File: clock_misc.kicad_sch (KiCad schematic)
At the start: 18 parts, among them J11 SPRING_CONTACT, J12 SPRING_CONTACT, J13 SPRING_CONTACT, J14 SPRING_CONTACT, J15 SPRING_CONTACT, J16 SPRING_CONTACT, Y1 Osc60MHz

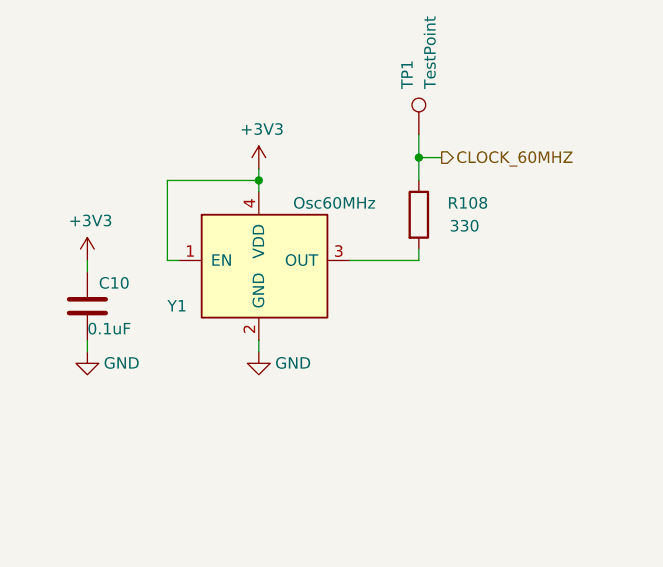
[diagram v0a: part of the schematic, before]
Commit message: Clean up schematic
- Renumber Pmod signal names to match silkscreen labels
- Clean up FPGA symbol
- Clean up PHY symbol
- Add title block to newer sheets
- Fix horizontal line in LED sheet
- Improve various label positions
- Update data sheet fields
- Renumber pages
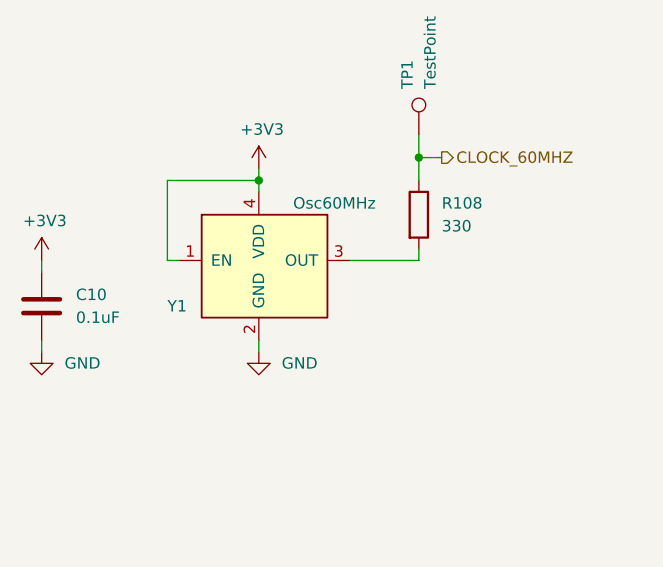
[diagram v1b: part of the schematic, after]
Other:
- company: (none) -> Copyright 2019-2023 Great Scott Gadgets
- title: (none) -> Cynthion
- moved on the sheet: C10
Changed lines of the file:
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@@
 (kicad_sch (version 20230121) (generator eeschema)
   (paper "A4")
+  (title_block
+    (title "Cynthion")
+    (date "${DATE}")
+    (rev "${VERSION}")
+    (company "Copyright 2019-2023 Great Scott Gadgets")
+    (comment 1 "Licensed under the CERN-OHL-P v2")
+  )
   (junction (at 73.66 67.31) (diameter 0) (color 0 0 0 0)
   )
@@
     (stroke (width 0) (type default))
   )
-  (wire (pts (xy 54.61 85.09) (xy 54.61 86.36))
+  (wire (pts (xy 49.53 85.09) (xy 49.53 86.36))
     (stroke (width 0) (type default))
   )
@@
     (stroke (width 0) (type default))
   )
-  (wire (pts (xy 54.61 76.2) (xy 54.61 77.47))
+  (wire (pts (xy 49.53 76.2) (xy 49.53 77.47))
     (stroke (width 0) (type default))
   )
@@
     (effects (font (size 1.27 1.27)) (justify left))
   )
-  (symbol (lib_id "Device:C") (at 54.61 81.28 0) (unit 1)
-    (in_bom yes) (on_board yes) (dnp no)
-    (property "Reference" "C10" (at 55.88 78.74 0)
-      (effects (font (size 1.27 1.27)) (justify left))
-    )
-    (property "Value" "0.1uF" (at 54.61 83.82 0)
-      (effects (font (size 1.27 1.27)) (justify left))
-    )
-    (property "Footprint" "Capacitor_SMD:C_0402_1005Metric" (at 55.5752 85.09 0)
-      (effects (font (size 1.27 1.27)) hide)
-    )
-    (property "Datasheet" "~" (at 54.61 81.28 0)
-      (effects (font (size 1.27 1.27)) hide)
-    )
-    (property "Part Number" "CL05A104KA5NNNC" (at 54.61 81.28 0)
-      (effects (font (size 1.27 1.27)) hide)
-    )
-    (property "Substitution" "any equivalent" (at 54.61 81.28 0)
-      (effects (font (size 1.27 1.27)) hide)
-    )
-    (property "Description" "CAP CER 0.1UF 25V X5R 0402" (at 54.61 81.28 0)
-      (effects (font (size 1.27 1.27)) hide)
-    )
-    (property "Manufacturer" "Samsung" (at 54.61 81.28 0)
+  (symbol (lib_id "Device:C") (at 49.53 81.28 0) (unit 1)
+    (in_bom yes) (on_board yes) (dnp no) (fields_autoplaced)
+    (property "Reference" "C10" (at 53.34 80.01 0)
+      (effects (font (size 1.27 1.27)) (justify left))
+    )
+    (property "Value" "0.1uF" (at 53.34 82.55 0)
+      (effects (font (size 1.27 1.27)) (justify left))
+    )
+    (property "Footprint" "Capacitor_SMD:C_0402_1005Metric" (at 50.4952 85.09 0)
+      (effects (font (size 1.27 1.27)) hide)
+    )
+    (property "Datasheet" "~" (at 49.53 81.28 0)
+      (effects (font (size 1.27 1.27)) hide)
+    )
+    (property "Part Number" "CL05A104KA5NNNC" (at 49.53 81.28 0)
+      (effects (font (size 1.27 1.27)) hide)
+    )
+    (property "Substitution" "any equivalent" (at 49.53 81.28 0)
+      (effects (font (size 1.27 1.27)) hide)
+    )
+    (property "Description" "CAP CER 0.1UF 25V X5R 0402" (at 49.53 81.28 0)
+      (effects (font (size 1.27 1.27)) hide)
+    )
+    (property "Manufacturer" "Samsung" (at 49.53 81.28 0)
       (effects (font (size 1.27 1.27)) hide)
     )
@@
       (effects (font (size 1.27 1.27)) hide)
     )
-    (property "Datasheet" "" (at 67.31 71.12 0)
+    (property "Datasheet" "https://www.sitime.com/datasheet/SiT1602" (at 67.31 71.12 0)
       (effects (font (size 1.27 1.27)) hide)
     )
@@
   )
   (symbol (lib_id "Device:R") (at 91.44 71.12 0) (unit 1)
-    (in_bom yes) (on_board yes) (dnp no)
-    (property "Reference" "R108" (at 94.615 69.85 0)
-      (effects (font (size 1.27 1.27)) (justify left))
-    )
-    (property "Value" "330" (at 96.52 72.39 0)
-      (effects (font (size 1.27 1.27)))
+    (in_bom yes) (on_board yes) (dnp no) (fields_autoplaced)
+    (property "Reference" "R108" (at 93.98 69.85 0)
+      (effects (font (size 1.27 1.27)) (justify left))
+    )
+    (property "Value" "330" (at 93.98 72.39 0)
+      (effects (font (size 1.27 1.27)) (justify left))
     )
     (property "Footprint" "Resistor_SMD:R_0402_1005Metric" (at 89.662 71.12 90)
@@
   )
   (symbol (lib_id "power:GND") (at 73.66 86.36 0) (unit 1)
-    (in_bom yes) (on_board yes) (dnp no)
+    (in_bom yes) (on_board yes) (dnp no) (fields_autoplaced)
     (property "Reference" "#PWR086" (at 73.66 92.71 0)
       (effects (font (size 1.27 1.27)) hide)
     )
-    (property "Value" "GND" (at 77.47 87.63 0)
-      (effects (font (size 1.27 1.27)))
+    (property "Value" "GND" (at 76.2 87.63 0)
+      (effects (font (size 1.27 1.27)) (justify left))
     )
     (property "Footprint" "" (at 73.66 86.36 0)
@@
     )
   )
-  (symbol (lib_id "power:GND") (at 54.61 86.36 0) (unit 1)
-    (in_bom yes) (on_board yes) (dnp no)
-    (property "Reference" "#PWR0174" (at 54.61 92.71 0)
-      (effects (font (size 1.27 1.27)) hide)
-    )
-    (property "Value" "GND" (at 58.42 87.63 0)
-      (effects (font (size 1.27 1.27)))
-    )
-    (property "Footprint" "" (at 54.61 86.36 0)
-      (effects (font (size 1.27 1.27)) hide)
-    )
-    (property "Datasheet" "" (at 54.61 86.36 0)
+  (symbol (lib_id "power:GND") (at 49.53 86.36 0) (unit 1)
+    (in_bom yes) (on_board yes) (dnp no) (fields_autoplaced)
+    (property "Reference" "#PWR0174" (at 49.53 92.71 0)
+      (effects (font (size 1.27 1.27)) hide)
+    )
+    (property "Value" "GND" (at 52.07 87.63 0)
+      (effects (font (size 1.27 1.27)) (justify left))
+    )
+    (property "Footprint" "" (at 49.53 86.36 0)
+      (effects (font (size 1.27 1.27)) hide)
+    )
+    (property "Datasheet" "" (at 49.53 86.36 0)
       (effects (font (size 1.27 1.27)) hide)
     )
@@
     )
   )
-  (symbol (lib_id "power:+3V3") (at 54.61 76.2 0) (unit 1)
-    (in_bom yes) (on_board yes) (dnp no)
-    (property "Reference" "#PWR018" (at 54.61 80.01 0)
-      (effects (font (size 1.27 1.27)) hide)
-    )
-    (property "Value" "+3V3" (at 54.9656 71.8058 0)
-      (effects (font (size 1.27 1.27)))
-    )
-    (property "Footprint" "" (at 54.61 76.2 0)
-      (effects (font (size 1.27 1.27)) hide)
-    )
-    (property "Datasheet" "" (at 54.61 76.2 0)
-      (effects (font (size 1.27 1.27)) hide)
-    )
+  (symbol (lib_id "power:+3V3") (at 49.53 76.2 0) (unit 1)
+    (in_bom yes) (on_board yes) (dnp no)
+    (property "Reference" "#PWR018" (at 49.53 80.01 0)
+      (effects (font (size 1.27 1.27)) hide)
+    )
+    (property "Value" "+3V3" (at 49.8856 71.8058 0)
+      (effects (font (size 1.27 1.27)))
+    )
+    (property "Footprint" "" (at 49.53 76.2 0)
+      (effects (font (size 1.27 1.27)) hide)
+    )
+    (property "Datasheet" "" (at 49.53 76.2 0)
+      (effects (font (size 1.27 1.27)) hide)
+    )

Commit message: Update copyright notices
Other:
- company: Copyright 2019-2023 Great Scott Gadgets -> ${COPYRIGHT}
- title: Cynthion -> ${TITLE}
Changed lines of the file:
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@@
   (paper "A4")
   (title_block
-    (title "Cynthion")
+    (title "${TITLE}")
     (date "${DATE}")
     (rev "${VERSION}")
-    (company "Copyright 2019-2023 Great Scott Gadgets")
-    (comment 1 "Licensed under the CERN-OHL-P v2")
+    (company "${COPYRIGHT}")
+    (comment 1 "${LICENSE}")
   )
   (junction (at 73.66 67.31) (diameter 0) (color 0 0 0 0)
